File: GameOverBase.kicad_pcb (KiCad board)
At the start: 4 copper layers, 50 x 35 mm, 47 parts, among them J1 USB_C_DEALON-USB-US31-106, J2 Serial Port, J3 add-on conn, Q1 PMN48XP, SW1 SW_DIP_x08, SW2 boot, SW3 Reset, U1 ESP32-WROOM-E, U2 4021, U3 MCP73831-2ACI-OT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

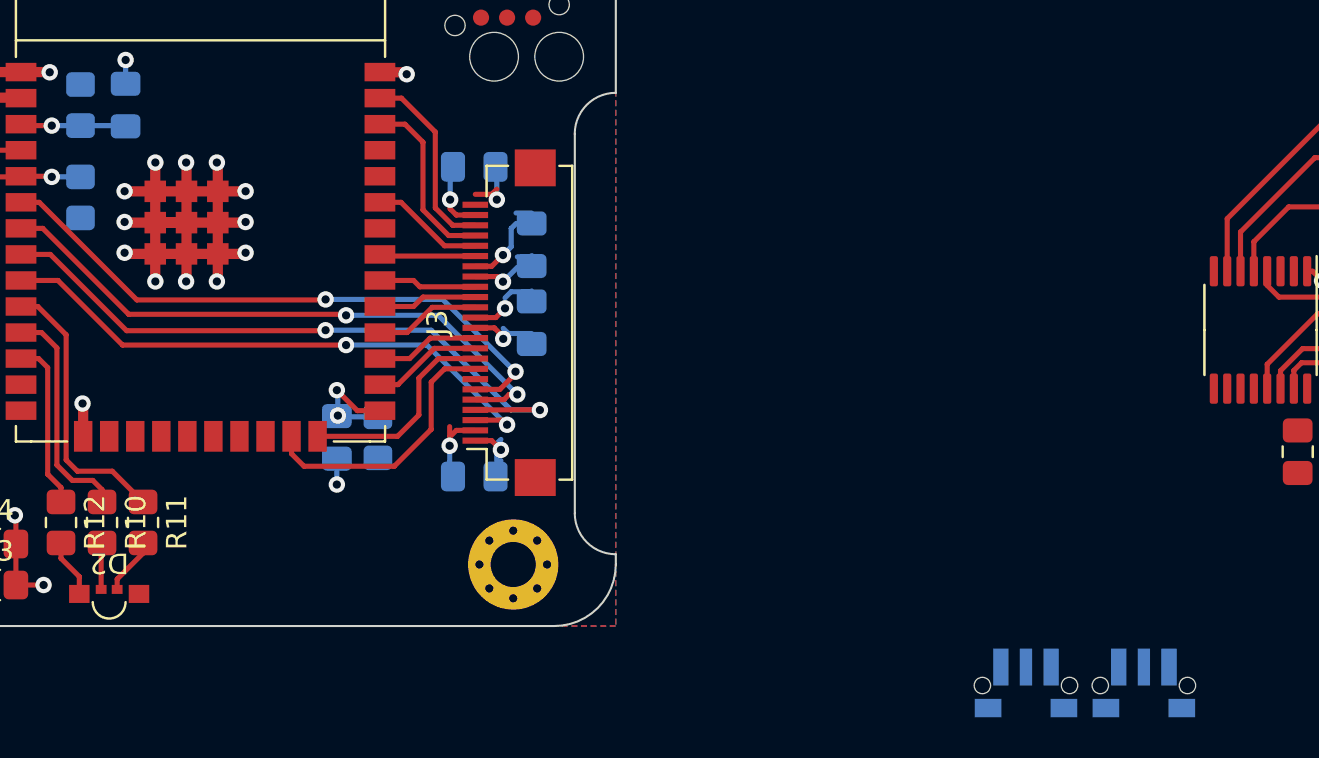
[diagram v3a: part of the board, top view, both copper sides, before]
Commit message: Routes boot and reset switches
I added a generic 3D model to the button footprint just to see how it
looks. Please note *this is no the actual button we'll use!
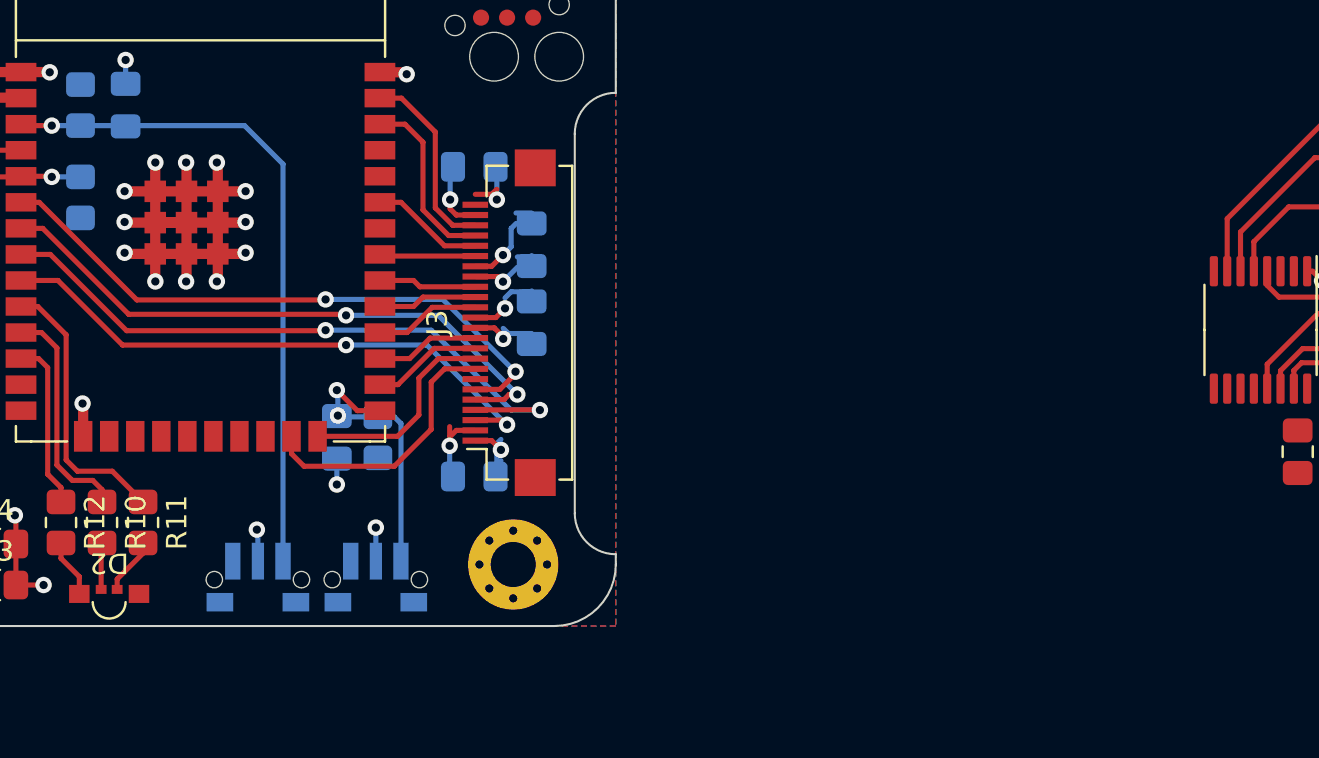
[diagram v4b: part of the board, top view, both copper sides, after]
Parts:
- moved SW2 37.8 mm to (158.3, 111.8)
- moved SW3 37.8 mm to (152.6, 111.8)
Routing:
- net ESP_EN: track 5.14 -> 33.0 mm
- net ESP_BOOT: track 5.75 -> 13.7 mm
- net GND: track 89.3 -> 92.5 mm, vias 38 -> 40
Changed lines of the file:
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@@
   )
   (footprint "GameOver:SW_Tactile_SPST_SOFNG_TS-1814" (layer "B.Cu")
-    (at 190 117 180)
+    (at 152.55 111.8375 180)
     (property "Sheetfile" "GameOverBase.kicad_sch")
     (property "Sheetname" "")
@@
     (pad "3" smd rect (at 1.225 0 180) (size 0.75 1.8) (layers "B.Cu" "B.Paste" "B.Mask")
       (thermal_bridge_angle 45))
+    (model "${KICAD6_3DMODEL_DIR}/Button_Switch_THT.3dshapes/SW_Tactile_SPST_Angled_PTS645Vx31-2LFS.wrl"
+      (offset (xyz 1.5 -1 0))
+      (scale (xyz 0.7 0.7 0.7))
+      (rotate (xyz 0 0 180))
+    )
   )
   (footprint "Resistor_SMD:R_0805_2012Metric_Pad1.20x1.40mm_HandSolder" (layer "B.Cu")
@@
   )
   (footprint "GameOver:SW_Tactile_SPST_SOFNG_TS-1814" (layer "B.Cu")
-    (at 195.75 117 180)
+    (at 158.3 111.8375 180)
     (property "Sheetfile" "GameOverBase.kicad_sch")
     (property "Sheetname" "")
@@
     (property "ki_keywords" "switch normally-open pushbutton push-button")
     (attr smd)
-    (fp_text reference "SW2" (at -24.25 0.75 90 unlocked) (layer "B.SilkS")
+    (fp_text reference "SW2" (at 0 2.8375 unlocked) (layer "B.SilkS")
         (effects (font (size 1 1) (thickness 0.15)) (justify mirror))
     )
@@
     (pad "3" smd rect (at 1.225 0 180) (size 0.75 1.8) (layers "B.Cu" "B.Paste" "B.Mask")
       (thermal_bridge_angle 45))
+    (model "${KICAD6_3DMODEL_DIR}/Button_Switch_THT.3dshapes/SW_Tactile_SPST_Angled_PTS645Vx31-2LFS.wrl"
+      (offset (xyz 1.5 -1 0))
+      (scale (xyz 0.7 0.7 0.7))
+      (rotate (xyz 0 0 180))
+    )
   )
   (footprint "GameOver:DIP-16_CTS_219-8LPST" (layer "B.Cu")
@@
   (via (at 142.4 88) (size 0.8) (drill 0.4) (layers "F.Cu" "B.Cu") (net 2))
   (via (at 151.95 93.8) (size 0.8) (drill 0.4) (layers "F.Cu" "B.Cu") (net 2))
+  (via (at 152.5 110.3) (size 0.8) (drill 0.4) (layers "F.Cu" "B.Cu") (net 2))
   (via (at 164.2 94.21) (size 0.8) (drill 0.4) (layers "F.Cu" "B.Cu") (net 2))
   (via (at 128.25 95.75) (size 0.8) (drill 0.4) (layers "F.Cu" "B.Cu") (net 2))
@@
   (via (at 122.9 94.8) (size 0.8) (drill 0.4) (layers "F.Cu" "B.Cu") (net 2))
   (via (at 140.7 109.6) (size 0.8) (drill 0.4) (layers "F.Cu" "B.Cu") (net 2))
+  (via (at 158.3 110.2) (size 0.8) (drill 0.4) (layers "F.Cu" "B.Cu") (net 2))
   (via (at 164.6 99.51) (size 0.8) (drill 0.4) (layers "F.Cu" "B.Cu") (net 2))
   (via (at 134.25 98) (size 0.8) (drill 0.4) (layers "F.Cu" "B.Cu") (net 2))
@@
   (segment (start 161.9 107.0375) (end 162.0625 107.2) (width 0.25) (layer "B.Cu") (net 2))
   (segment (start 164.9 98.7) (end 165.8625 98.7) (width 0.25) (layer "B.Cu") (net 2))
+  (segment (start 152.55 111.8375) (end 152.55 110.35) (width 0.25) (layer "B.Cu") (net 2))
   (segment (start 164.9 96.51) (end 164.9 95.61) (width 0.25) (layer "B.Cu") (net 2))
+  (segment (start 152.55 110.35) (end 152.5 110.3) (width 0.25) (layer "B.Cu") (net 2))
+  (segment (start 158.3 111.8375) (end 158.3 110.2) (width 0.25) (layer "B.Cu") (net 2))
   (segment (start 164.9 95.61) (end 165.1375 95.3725) (width 0.25) (layer "B.Cu") (net 2))
   (segment (start 146.1 88.5625) (end 146.1 87.4) (width 0.25) (layer "B.Cu") (net 2))
@@
   (via (at 156.449473 104.738521) (size 0.8) (drill 0.4) (layers "F.Cu" "B.Cu") (net 4))
   (via (at 156.4 103.5) (size 0.8) (drill 0.4) (layers "F.Cu" "B.Cu") (net 4))
+  (segment (start 159.525 105.125) (end 159.2 104.8) (width 0.25) (layer "B.Cu") (net 4))
+  (segment (start 159.525 111.8375) (end 159.525 105.125) (width 0.25) (layer "B.Cu") (net 4))
   (segment (start 158.4 104.8) (end 156.510952 104.8) (width 0.25) (layer "B.Cu") (net 4))
   (segment (start 156.510952 104.8) (end 156.449473 104.738521) (width 0.25) (layer "B.Cu") (net 4))
+  (segment (start 159.2 104.8) (end 158.4 104.8) (width 0.25) (layer "B.Cu") (net 4))
   (segment (start 156.449473 104.738521) (end 156.449473 103.549473) (width 0.25) (layer "B.Cu") (net 4))
   (segment (start 156.449473 103.549473) (end 156.4 103.5) (width 0.25) (layer "B.Cu") (net 4))
@@
   (segment (start 142.5 90.6) (end 141.07 90.6) (width 0.25) (layer "F.Cu") (net 5))
   (via (at 142.5 90.6) (size 0.8) (drill 0.4) (layers "F.Cu" "B.Cu") (net 5))
+  (segment (start 153.775 92.475) (end 151.9 90.6) (width 0.25) (layer "B.Cu") (net 5))
   (segment (start 143.9 90.6) (end 146.0625 90.6) (width 0.25) (layer "B.Cu") (net 5))
+  (segment (start 151.9 90.6) (end 146.1375 90.6) (width 0.25) (layer "B.Cu") (net 5))
   (segment (start 143.9 90.6) (end 142.5 90.6) (width 0.25) (layer "B.Cu") (net 5))
+  (segment (start 146.1375 90.6) (end 146.1 90.6375) (width 0.25) (layer "B.Cu") (net 5))
   (segment (start 146.0625 90.6) (end 146.1 90.6375) (width 0.25) (layer "B.Cu") (net 5))
+  (segment (start 153.775 111.8375) (end 153.775 92.475) (width 0.25) (layer "B.Cu") (net 5))
   (segment (start 138.3375 91.6) (end 139.3 91.6) (width 0.5) (layer "F.Cu") (net 6))
   (segment (start 139.5 91.8) (end 141 91.8) (width 0.25) (layer "F.Cu") (net 6))

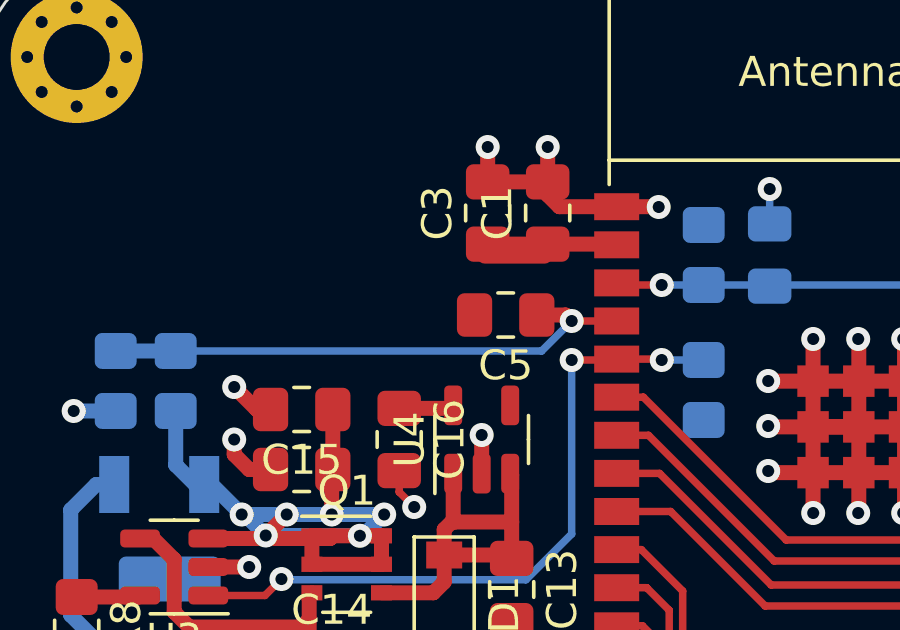
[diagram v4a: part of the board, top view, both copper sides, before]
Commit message: Adds missing GND connection the te battery sense decoupling cap
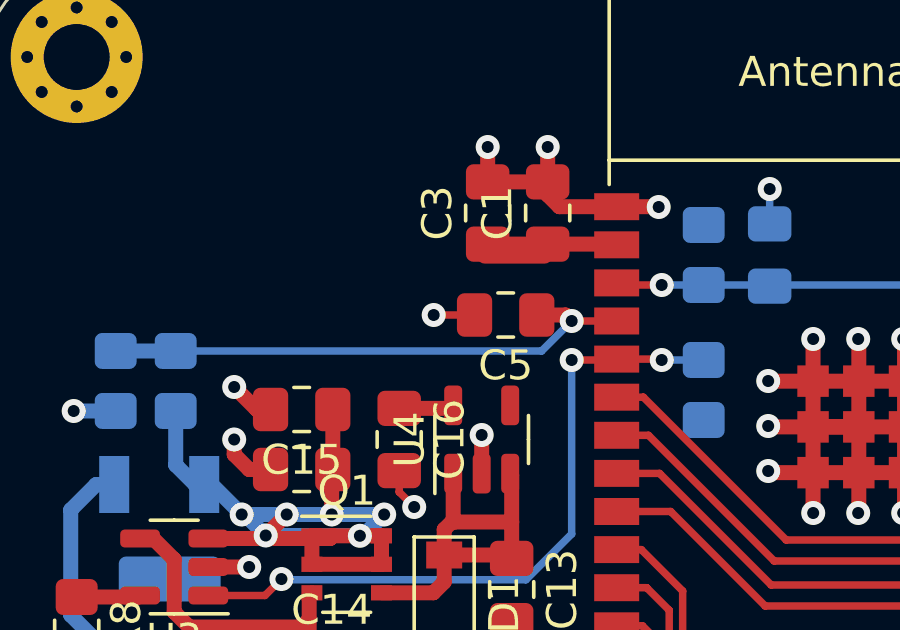
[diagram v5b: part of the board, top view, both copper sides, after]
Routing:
- net GND: track 92.5 -> 93.9 mm, vias 40 -> 41
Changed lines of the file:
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@@
   (segment (start 161.9 105.275978) (end 161.9 105.7) (width 0.25) (layer "F.Cu") (net 2))
   (segment (start 141 87.99) (end 139.09 87.99) (width 0.5) (layer "F.Cu") (net 2))
+  (segment (start 136.2625 91.6) (end 134.9 91.6) (width 0.25) (layer "F.Cu") (net 2))
   (segment (start 142.4 88) (end 142.39 87.99) (width 0.5) (layer "F.Cu") (net 2))
   (segment (start 163.15 99.96) (end 164.15 99.96) (width 0.25) (layer "F.Cu") (net 2))
@@
   (via (at 129.5 108.25) (size 0.8) (drill 0.4) (layers "F.Cu" "B.Cu") (net 2))
   (via (at 147.55 92.4) (size 0.8) (drill 0.4) (layers "F.Cu" "B.Cu") (net 2))
+  (via (at 134.9 91.6) (size 0.8) (drill 0.4) (layers "F.Cu" "B.Cu") (net 2))
   (via (at 122.9 94.8) (size 0.8) (drill 0.4) (layers "F.Cu" "B.Cu") (net 2))
   (via (at 140.7 109.6) (size 0.8) (drill 0.4) (layers "F.Cu" "B.Cu") (net 2))

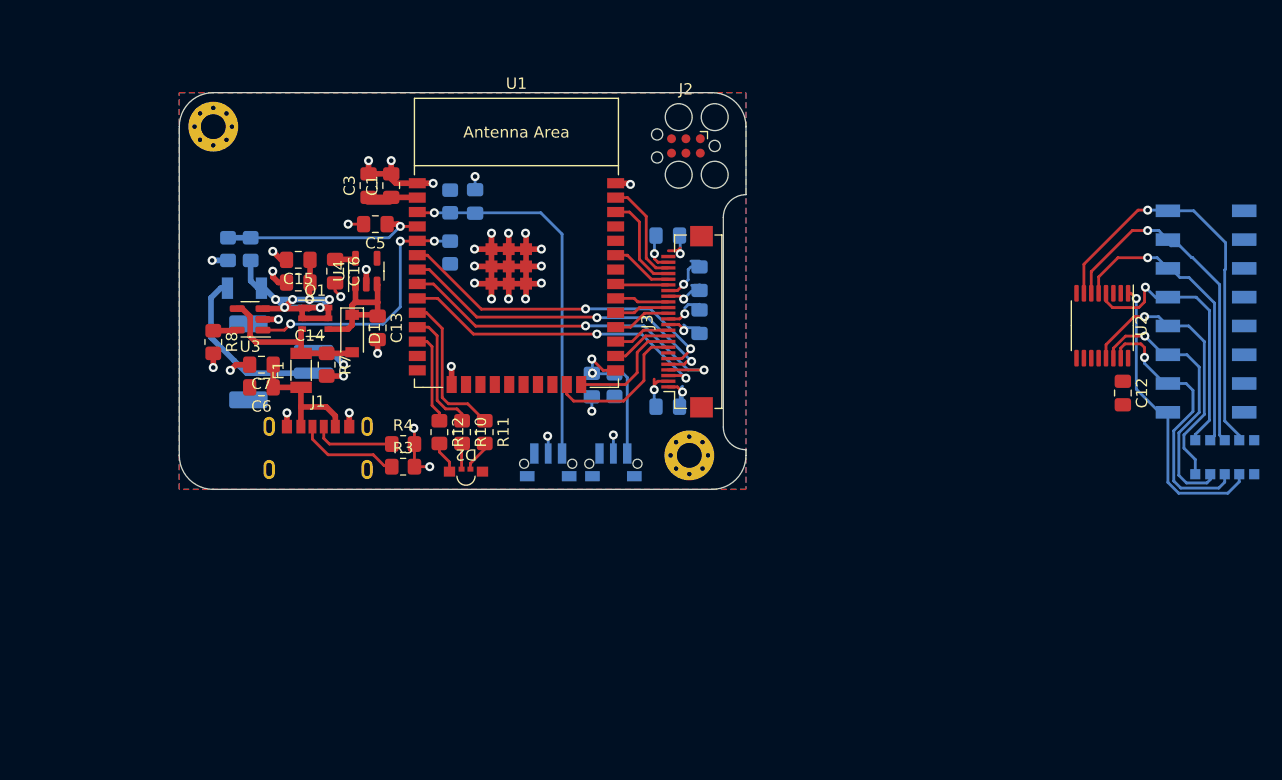
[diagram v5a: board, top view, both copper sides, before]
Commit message: Reorganizes power section so we have more space for the DIP switches
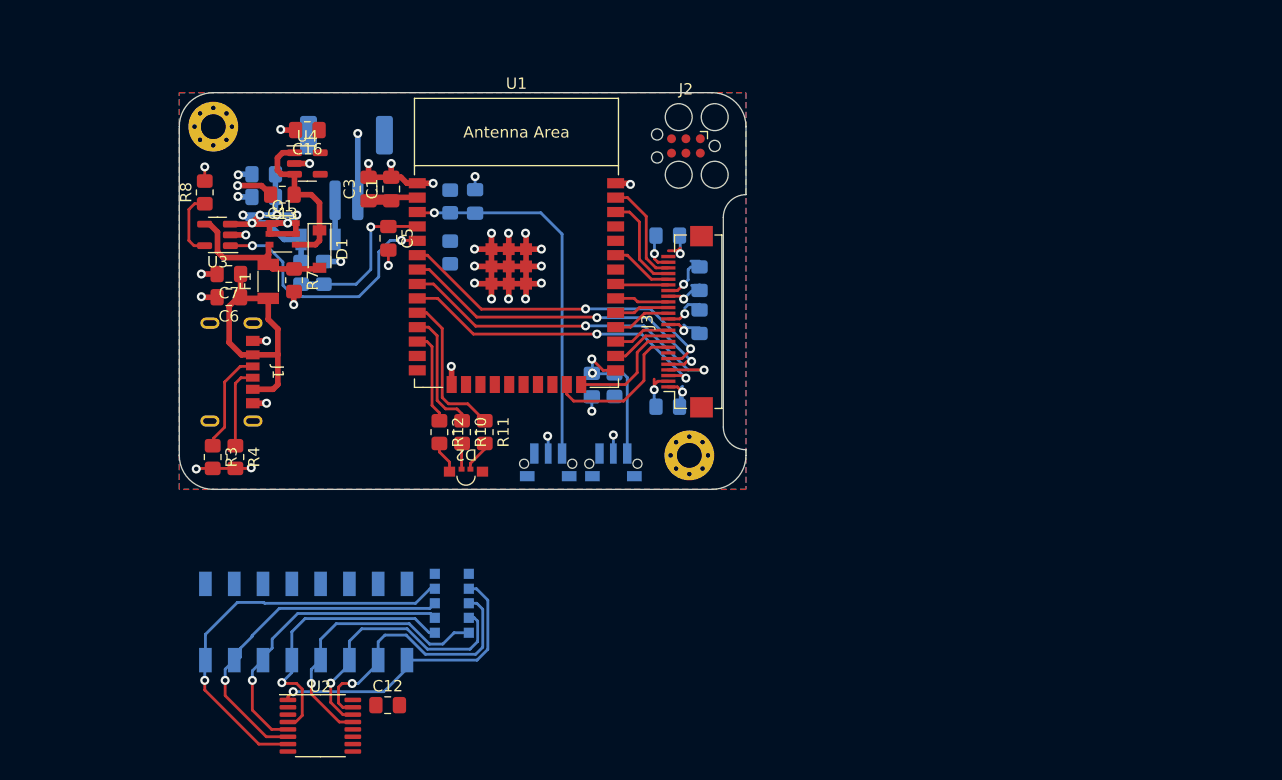
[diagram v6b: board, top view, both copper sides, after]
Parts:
- C14, C15: moved to B.Cu
- moved SW1 84.0 mm to (131.2, 126.7), turned to -90 degrees
- moved U2 77.5 mm to (132.4, 135.8), turned to 0 degrees
- moved C12 70.5 mm to (138.4, 134.0), turned to 0 degrees
- moved RN1 69.4 mm to (144.1, 125.0), turned to 180 degrees
- moved BT1 18.0 mm to (134.8, 86.7), turned to 0 degrees
- moved R3 16.8 mm to (123.0, 112.2), turned to -90 degrees
- moved R4 14.8 mm to (125.0, 112.2), turned to -90 degrees
- moved C13 14.4 mm to (129.1, 89.0), turned to 180 degrees
- moved R8 13.2 mm to (122.2, 88.8), turned to 90 degrees
- moved C16 12.7 mm to (131.3, 83.3), turned to 180 degrees
- moved J1 11.4 mm to (123.7, 104.7), turned to -90 degrees
- moved U4 10.8 mm to (131.3, 86.2), turned to 0 degrees
- moved C14 10.0 mm to (127.5, 87.2)
- moved R6 8.71 mm to (132.8, 95.9), turned to 90 degrees
- moved C7 8.50 mm to (124.4, 96.0)
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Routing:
- net Net-(BT1-+): track 15.7 -> 3.45 mm
- net Net-(J1-VBUS): track 12.2 -> 24.2 mm
- net GND: track 93.9 -> 98.1 mm, vias 41 -> 42
- net BAT_SENSE: track 18.5 -> 14.6 mm
- net Net-(U3-PROG): track 2.13 -> 5.93 mm
- net +3V3: track 21.1 -> 19.4 mm
- net +BATT: track 30.1 -> 31.6 mm
- net VCC: track 13.1 -> 14.3 mm
- net BAT_STAT: track 23.2 -> 22.9 mm, vias 3 -> 2
